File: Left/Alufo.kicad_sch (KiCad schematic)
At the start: 27 parts, among them J1 USB_C_Receptacle_USB2.0_16P_2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, J3 USB_C_Receptacle_USB2.0_16P_2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, SW1 BOOT, U1 CH552T, U3 USBLC6-2P6, U5 USBLC6-2P6

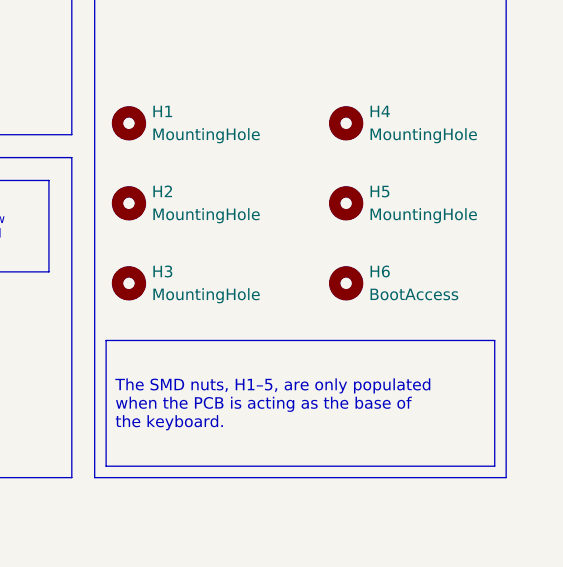
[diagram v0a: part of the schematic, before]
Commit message: Revert boot access hole change
It was correct before!
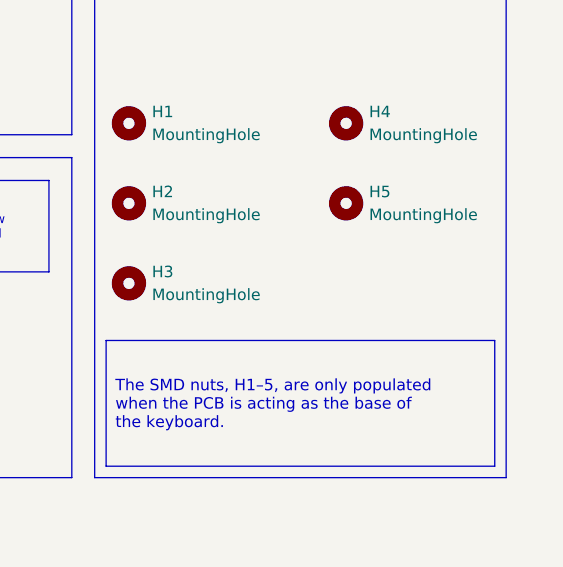
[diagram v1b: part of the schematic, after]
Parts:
- removed H6: BootAccess, MountingHole:MountingHole_2.5mm, symbol Mechanical:MountingHole
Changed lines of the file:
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@@
-	(symbol
-		(lib_id "Mechanical:MountingHole")
-		(at 177.8 214.63 0)
-		(unit 1)
-		(exclude_from_sim yes)
-		(in_bom no)
-		(on_board yes)
-		(dnp no)
-		(fields_autoplaced yes)
-		(property "Reference" "H6"
-			(at 180.34 213.3599 0)
-			(effects
-				(font
-					(size 1.27 1.27)
-				)
-				(justify left)
-			)
-		)
-		(property "Value" "BootAccess"
-			(at 180.34 215.8999 0)
-			(effects
-				(font
-					(size 1.27 1.27)
-				)
-				(justify left)
-			)
-		)
-		(property "Footprint" "MountingHole:MountingHole_2.5mm"
-			(at 177.8 214.63 0)
-			(effects
-				(font
-					(size 1.27 1.27)
-				)
-				(hide yes)
-			)
-		)
-		(property "Datasheet" "~"
-			(at 177.8 214.63 0)
-			(effects
-				(font
-					(size 1.27 1.27)
-				)
-				(hide yes)
-			)
-		)
-		(property "Description" "Mounting Hole without connection"
-			(at 177.8 214.63 0)
-			(effects
-				(font
-					(size 1.27 1.27)
-				)
-				(hide yes)
-			)
-		)
-		(instances
-			(project "Alufo"
-				(path "/52f043ac-ccff-4c85-bc10-2db9d3c9e3f3"
-					(reference "H6")
-					(unit 1)
-				)
-			)
-		)
-	)
 	(symbol
 		(lib_id "Mechanical:MountingHole")

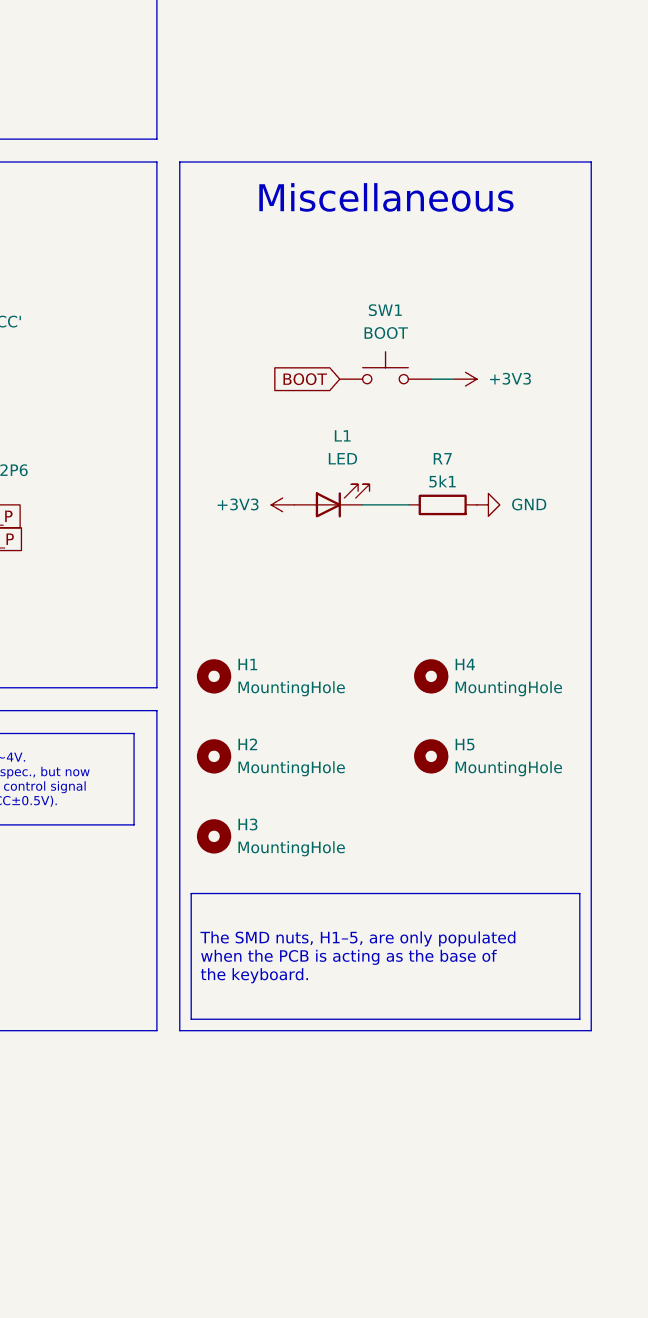
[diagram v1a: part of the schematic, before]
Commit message: Add lefthand plate
The plate file is arranged to the left of the main PCB. This arrangement is a little more costly  than if the plate were upside down under the PCB. However, the cost difference is small (~$3 for a five-PCB run) and this way makes it easier to crosscheck and make matching adjustments to the plate and the PCB.
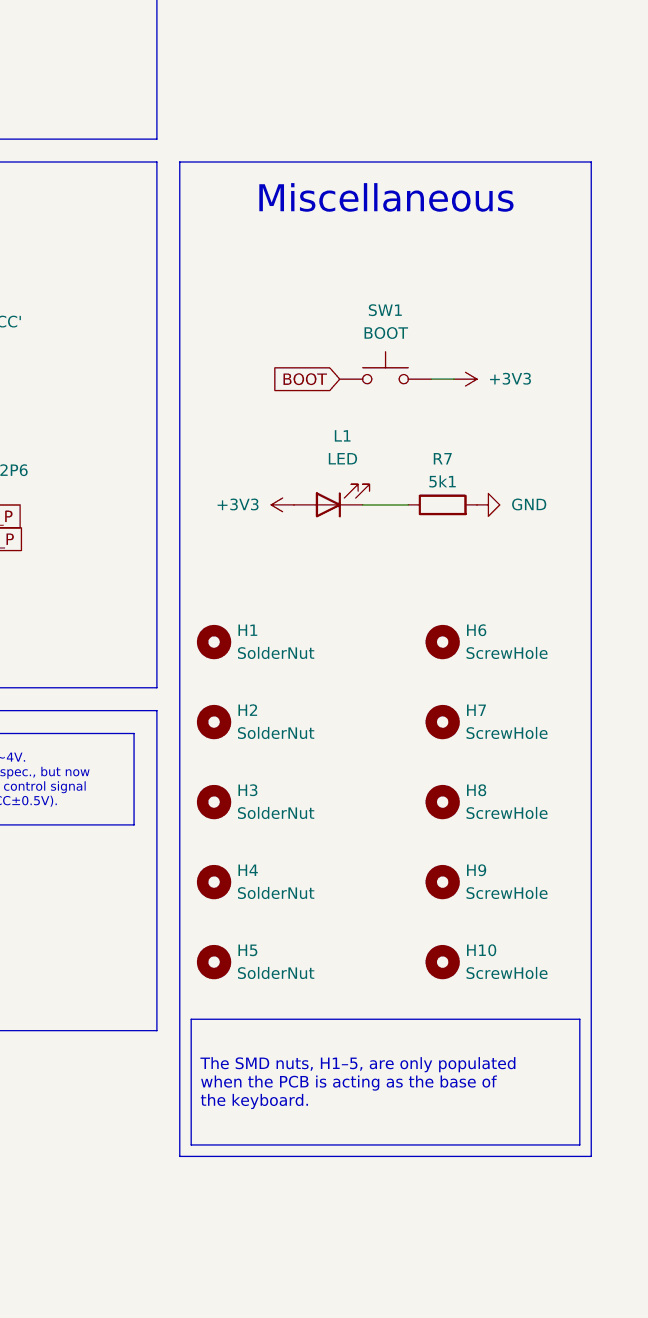
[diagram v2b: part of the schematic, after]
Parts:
- added H10, H6, H7, H8, H9: ScrewHole, MountingHole:MountingHole_2.2mm_M2, symbol Mechanical:MountingHole
- H1, H2, H3, H4, H5: value MountingHole -> SolderNut
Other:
- moved on the sheet: H1, H2, H3, H4, H5

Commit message: Connect aluminium back to copper layer
Holes J5 and J6 will be filled with solder on the active PCB to connect the back aluminium layer (which is connected to the USB shield) with the mounting hole H3. H3 will in turn connect to the bottom layer PCB via the solder nut pressed against the exposed pad on the active PCB. The solder nut will connect to the screw and the screw will connect to the top plate. The upper middle plate will connect to the shield by virtue of being physically pressed to the active PCB’s back (if correctly oriented).
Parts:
- added J5: SolderHole, TestPoint:TestPoint_THTPad_D2.5mm_Drill1.2mm, symbol Connector:Conn_01x01_Socket
- H3: footprint Project Library:MountingHole_2.2mm_M2_SMD_Solder_Nut -> Project Library:MountingHole_2.2mm_M2_SMD_Solder_Nut_Pad; symbol Mechanical:MountingHole -> Mechanical:MountingHole_Pad
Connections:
- new net Shield: H3.1, J5.1 (Pin_1)
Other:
- moved on the sheet: L1, R7, SW1

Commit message: Do not exclude solder nuts from BOM
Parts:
- H1, H2, H3, H4, H5: now in the parts list
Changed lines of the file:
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@@
 		(unit 1)
 		(exclude_from_sim yes)
-		(in_bom no)
+		(in_bom yes)
 		(on_board yes)
 		(dnp no)
@@
 		(unit 1)
 		(exclude_from_sim yes)
-		(in_bom no)
+		(in_bom yes)
 		(on_board yes)
 		(dnp no)
@@
 		(unit 1)
 		(exclude_from_sim yes)
-		(in_bom no)
+		(in_bom yes)
 		(on_board yes)
 		(dnp no)
@@
 		(unit 1)
 		(exclude_from_sim yes)
-		(in_bom no)
+		(in_bom yes)
 		(on_board yes)
 		(dnp no)
@@
 		(unit 1)
 		(exclude_from_sim yes)
-		(in_bom no)
+		(in_bom yes)
 		(on_board yes)
 		(dnp no)

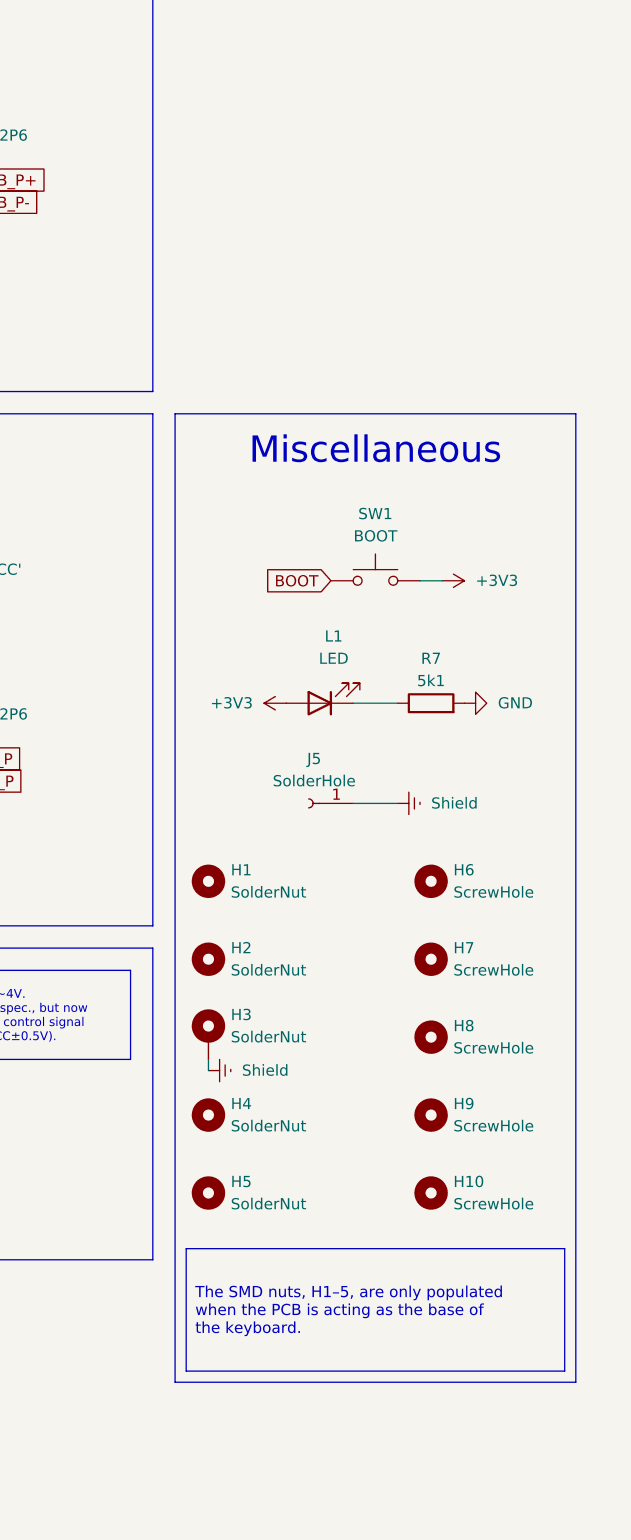
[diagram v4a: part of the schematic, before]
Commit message: Update link between PCB and plate
There are now two connections, with mouse bites at both ends.
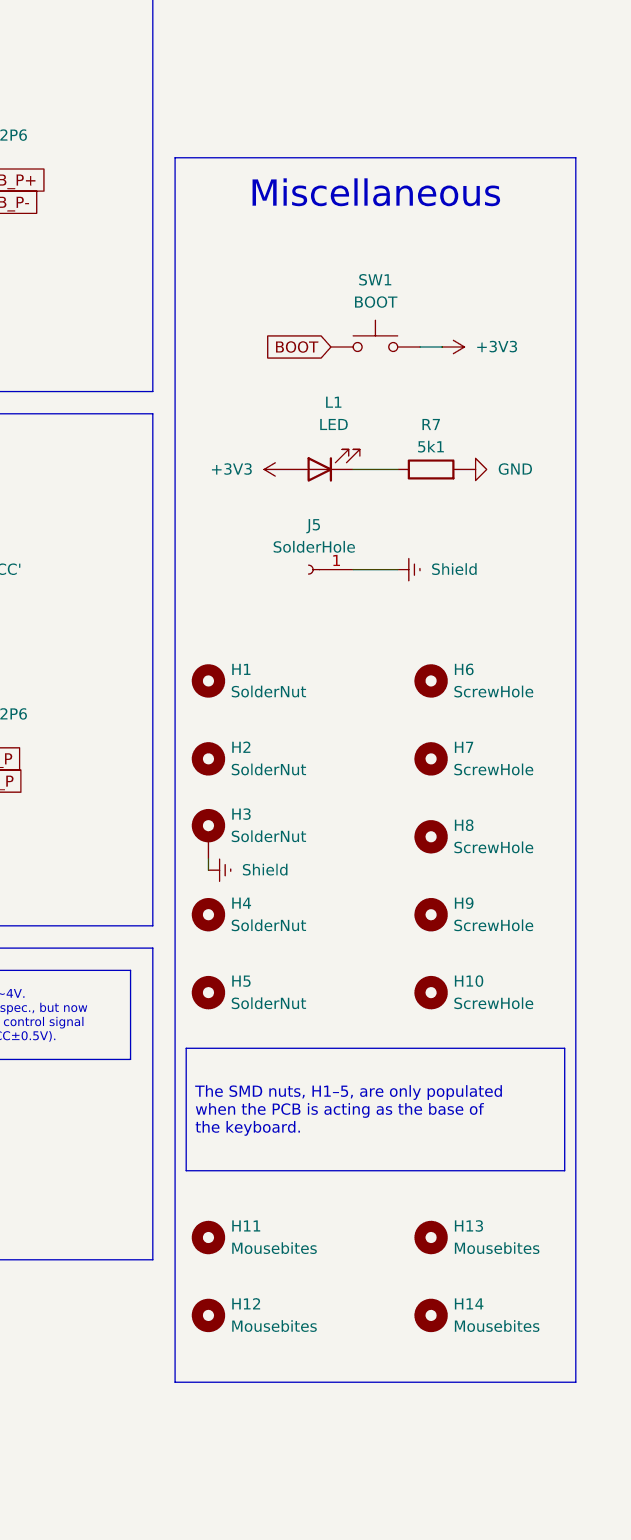
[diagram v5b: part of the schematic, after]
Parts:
- added H11, H12, H13, H14: Mousebites, Project Library:Mousebites, symbol Mechanical:MountingHole
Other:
- moved on the sheet: H1, H10, H2, H3, H4, H5, H6, H7, H8, H9, J5, L1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
